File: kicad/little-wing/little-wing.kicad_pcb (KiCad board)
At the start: 4 copper layers, 14 x 42.1 mm, 69 parts, among them J1 HRO_TYPE-C-31-M-14, J2 Battery, J3 rgb, J4 columns, J5 Conn_01x10, J6 rows, J7 sensor, J8 Conn_ARM_SWD_TagConnect_TC203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, Q1 AO3401A, Q2 2N7002, SW1 Battery, SW2 Reset, U1 nRF52840_CKAA, U2 nPM1100-CAAx, X1 32MHz, X2 32.768kHz

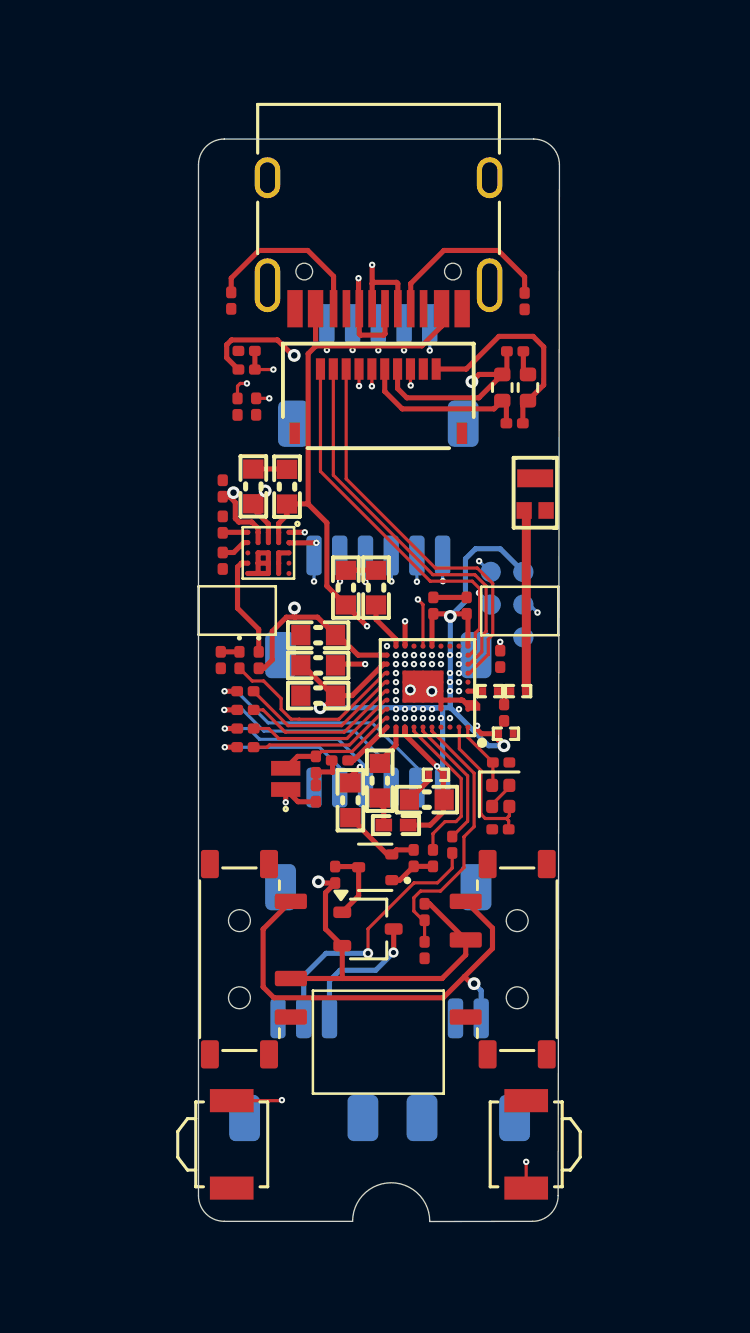
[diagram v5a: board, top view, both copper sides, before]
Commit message: Adding the solid ground fill
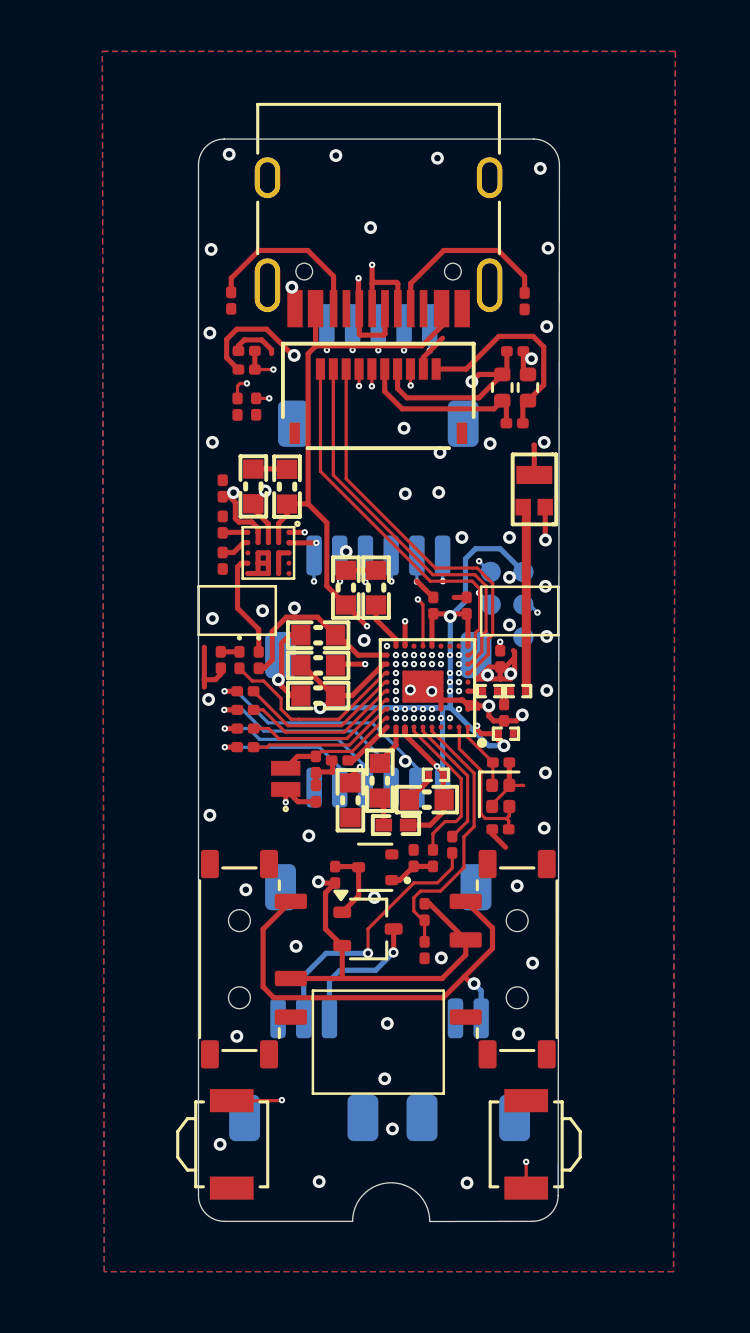
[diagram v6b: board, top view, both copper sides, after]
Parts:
- moved AE1 0.13 mm to (156.1, 71.3)
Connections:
- AE1 pad 2: (no net) -> GND
- X1 pad 2: unconnected-(X1-GND-Pad2) -> GND
- X1 pad 4: unconnected-(X1-GND-Pad4) -> GND
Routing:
- net GND: track 20.6 -> 40.2 mm, vias 4 -> 59
- net VDD: track 64.8 -> 72.8 mm
- added copper zone on B.Cu, net GND
- added copper zone on F.Cu, net GND
- added copper zone on In1.Cu, net GND
- added copper zone on In2.Cu, net GND

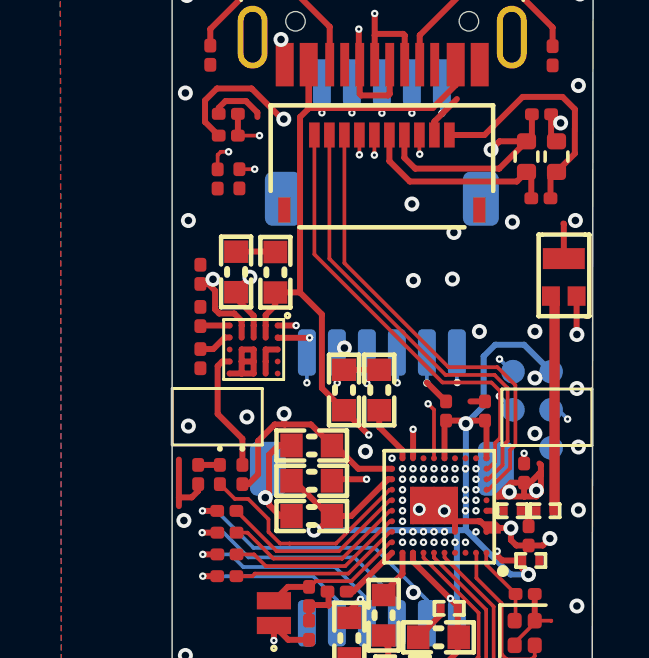
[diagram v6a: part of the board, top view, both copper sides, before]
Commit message: Adding the Plan B pins
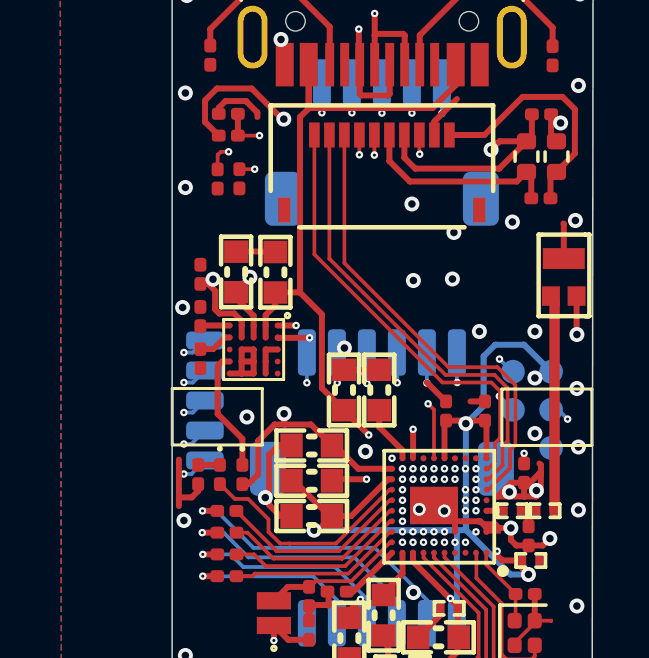
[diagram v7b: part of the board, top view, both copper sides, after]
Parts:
- added J9: Conn_01x05_Pin, Connector_JST:JST_SHL_SM05B-SHLS-TF_1x05-1MP_P1.00mm_Horizontal, B.Cu at (145.8, 75.4)
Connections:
- AE1 pad 2: GND -> (no net)
- U1 pad C9: unconnected-(U1-P0.26-PadC9) -> PlanB 5
- U1 pad D9: unconnected-(U1-P0.27-PadD9) -> PlanB 4
- U1 pad E9: unconnected-(U1-P0.06-PadE9) -> PlanB 3
- U1 pad F9: unconnected-(U1-P0.07-PadF9) -> PlanB 2
- U1 pad G9: unconnected-(U1-P1.08-PadG9) -> PlanB 1
- X1 pad 2: GND -> unconnected-(X1-GND-Pad2)
- X1 pad 4: GND -> unconnected-(X1-GND-Pad4)
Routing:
- net PlanB 1: track 0.00 -> 10.6 mm, vias 0 -> 2
- net PlanB 2: track 0.00 -> 9.98 mm, vias 0 -> 2
- net PlanB 3: track 0.00 -> 9.51 mm, vias 0 -> 2
- net PlanB 4: track 0.00 -> 9.24 mm, vias 0 -> 2
- net PlanB 5: track 0.00 -> 8.97 mm, vias 0 -> 2
- net unconnected-(U1-P1.08-PadG9): vias 1 -> 0
- net unconnected-(U1-P0.27-PadD9): vias 1 -> 0
- net unconnected-(U1-P0.26-PadC9): vias 1 -> 0
- net unconnected-(U1-P0.07-PadF9): vias 1 -> 0
- net unconnected-(U1-P0.06-PadE9): vias 1 -> 0
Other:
- board text added: "Battery"
- board text added: "Columns"
- board text added: "Plan B ->"
- board text added: "RGB"
- board text added: "Rows"
- board text added: "Sensor"

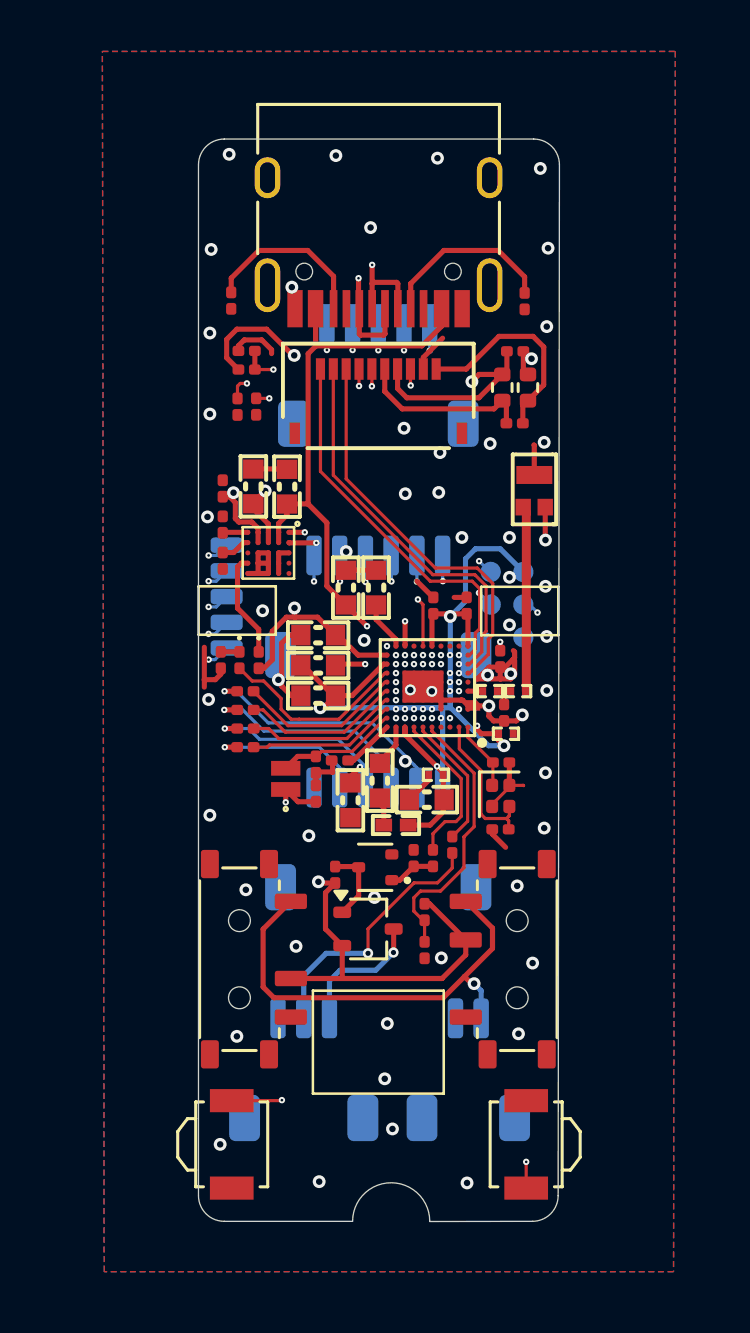
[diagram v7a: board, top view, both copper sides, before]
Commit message: Reworking the RGB power section
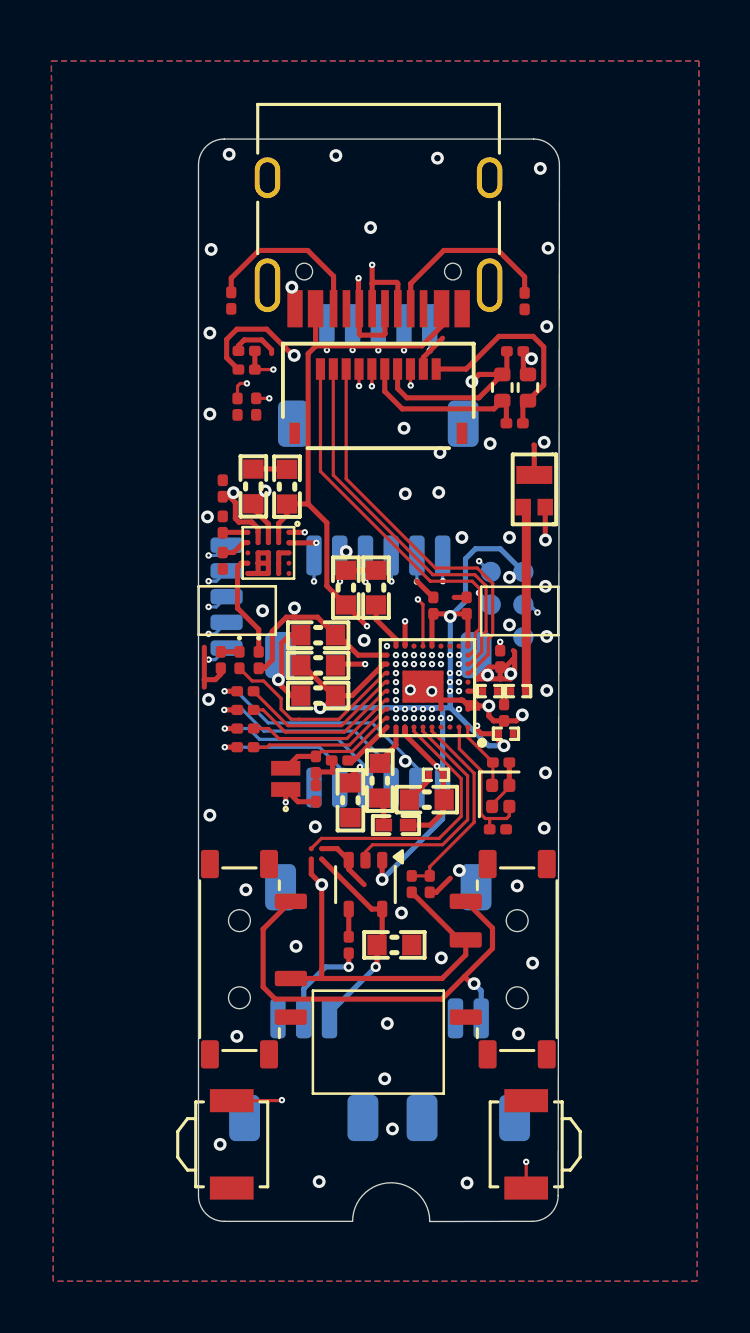
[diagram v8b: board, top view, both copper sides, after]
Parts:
- removed Q1: AO3401A, Package_TO_SOT_SMD:SOT-323_SC-70
- removed Q2: 2N7002, Package_TO_SOT_SMD:SOT-523
- removed R10, R18: 10k, Resistor_SMD:R_0201_0603Metric
- removed R17: 100R, Resistor_SMD:R_0201_0603Metric
- added C4: 10µF, Passive:CAPC1608X06L, F.Cu at (150.6, 88.9)
- added U3: TPS22916BYFPT, TPS22916 load switch:BGA4C40P2X2_77X77X50, F.Cu at (147.6, 85.4)
- added U4: SN74LV1T125DCK, Package_TO_SOT_SMD:SOT-353_SC-70-5, F.Cu at (149.5, 86.6)
- moved R8 5.60 mm to (148.8, 89.0)
- moved R_DIV2 2.57 mm to (152.0, 86.6)
- moved R_DIV1 1.19 mm to (151.3, 86.6), turned to 90 degrees
- moved C2 0.10 mm to (154.7, 84.5), turned to 0 degrees
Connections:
- net /Main Module/MCU/RF renamed /MCU/RF
- net /Main Module/PSU/CHG renamed /PSU/CHG
- J1 pad A6: D- -> D+
- J1 pad A7: D+ -> D-
- J1 pad B6: D- -> D+
- J1 pad B7: D+ -> D-
- J3 pad 1: RGB_POWER -> Net-(J3-Pin_1)
- R8 pad 1: RGB DATA -> Net-(U4-Y)
- U2 pad A1: D+ -> D-
- U2 pad A2: D- -> D+
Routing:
- net Net-(J3-Pin_1): track 0.00 -> 7.84 mm, vias 0 -> 1
- net Net-(J3-Pin_2): track 10.3 -> 3.78 mm
- net RGB_POWER: track 5.32 -> 0.00 mm, vias 1 -> 0
- net VDD: track 72.8 -> 78.1 mm, vias 9 -> 10
- net RGB ON: track 6.24 -> 10.6 mm
- net RGB DATA: track 5.22 -> 9.14 mm
- net Net-(Q1-G): track 2.94 -> 0.00 mm
- net VSENSE: track 10.7 -> 7.86 mm
- net GND: track 40.2 -> 42.2 mm, vias 59 -> 60
- net Net-(Q2-G): track 1.82 -> 0.00 mm
- net Net-(U4-Y): track 0.00 -> 1.08 mm
- net VBAT: track 34.4 -> 35.2 mm
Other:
- board text added: "PlanB»"
- board text added: "v1.0 by KaiBoards"
- board text removed: "Plan B ->"
